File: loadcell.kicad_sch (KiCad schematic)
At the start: 11 parts, among them J31 DSUB_15pin/VGA Veritical Fema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, U33 INA126

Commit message: GSE v2.1 done, just waiting on prop rn to finalize their sensor list
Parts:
- removed U33: INA126, Package_SO:SOIC-8_3.9x4.9mm_P1.27mm, symbol Amplifier_Instrumentation:INA128
- added U33: INA126, 0UCIRP-KiCAD-Lib:Instrumentation_Amplifiers INA126, symbol 0UCIRP-KiCAD-Lib:Instrumentation_Amplifiers INA126
- renumbered C130 to C91
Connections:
- net +5V: now also U33.7 (V+)
- net AO: now also U33.6
- net GND: now also U33.4 (V-), U33.5 (Ref)
- net at R172.2: now also U33.1 (Rg)
- net at C88.2, C90.1, R169.2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: now also U33.2 (-)
- net at C88.1, C89.2, R168.1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: now also U33.3 (+)
- net at R172.1: now also U33.8 (Rg)

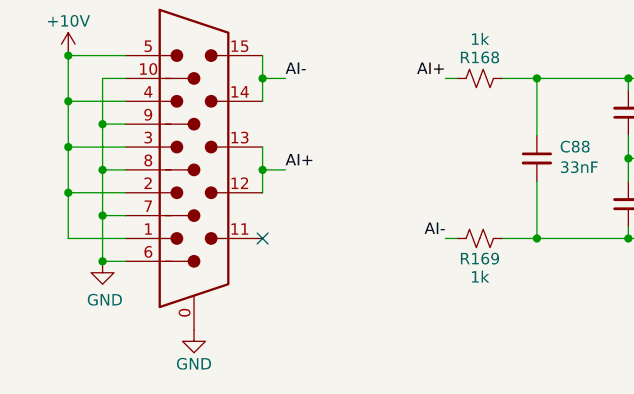
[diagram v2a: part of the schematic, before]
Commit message: GSEv2.1: changed pinout for PT and Loadcell where pin11 on VGA is grounded
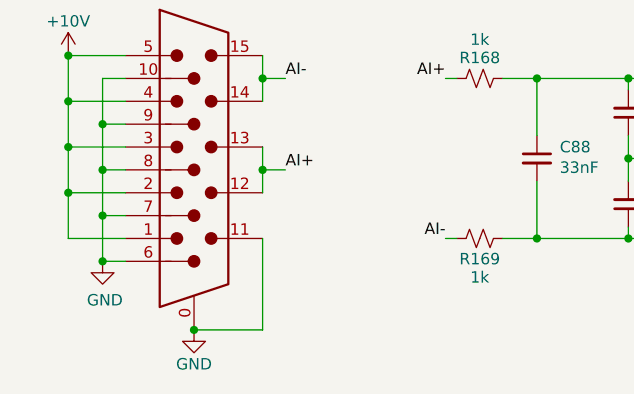
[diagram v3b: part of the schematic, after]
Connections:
- net GND: now also J31.11
- no-connect marks 1 -> 0
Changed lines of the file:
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@@
+	)
+	(junction
+		(at 100.33 132.08)
+		(diameter 0)
+		(color 0 0 0 0)
 	)
 	(junction
@@
 		(color 0 0 0 0)
 	)
-	(no_connect
-		(at 107.95 121.92)
-	)
 	(wire
 		(pts
@@
 	(wire
 		(pts
+			(xy 107.95 132.08) (xy 100.33 132.08)
+		)
+		(stroke
+			(width 0)
+			(type default)
+		)
+	)
+	(wire
+		(pts
 			(xy 128.27 121.92) (xy 129.54 121.92)
 		)
@@
 		)
 		(stroke
+			(width 0)
+			(type default)
+		)
+	)
+	(wire
+		(pts
+			(xy 107.95 121.92) (xy 107.95 132.08)
+		)
+		(stroke

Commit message: GSE v2.1: Done, ready for JLCPCB
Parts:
- renumbered R168 to R171, R169 to R172, R170 to R173, R171 to R174, R172 to R175
